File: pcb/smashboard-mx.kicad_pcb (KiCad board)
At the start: 2 copper layers, 139.1 x 76.2 mm, 87 parts, among them J1 OLED_128x32_Nice_View, SW1 SW_SPDT, SW2 SW_Push, SW3 SW_SPDT, SW4 SW_Push, U1 Nice_Nano_V2

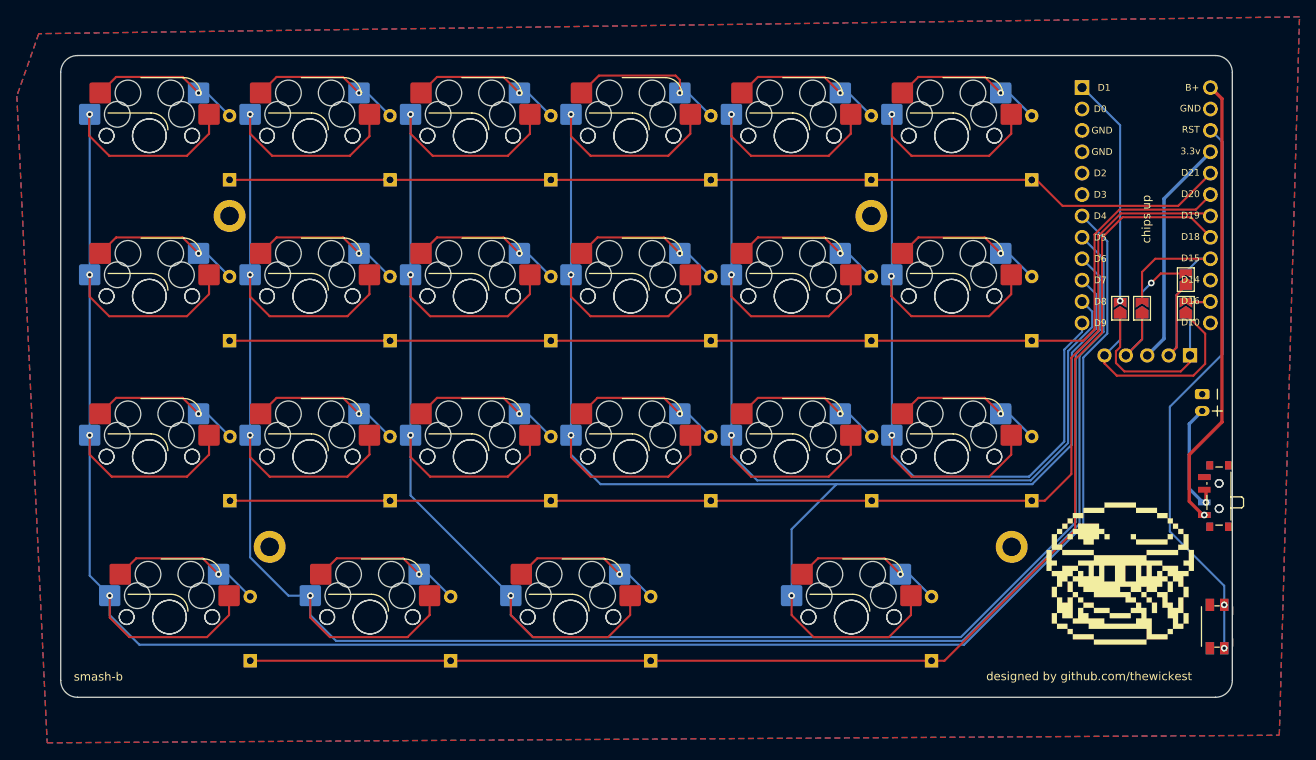
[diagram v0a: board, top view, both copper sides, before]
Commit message: Move 2u diode to the side. Interference with the stab
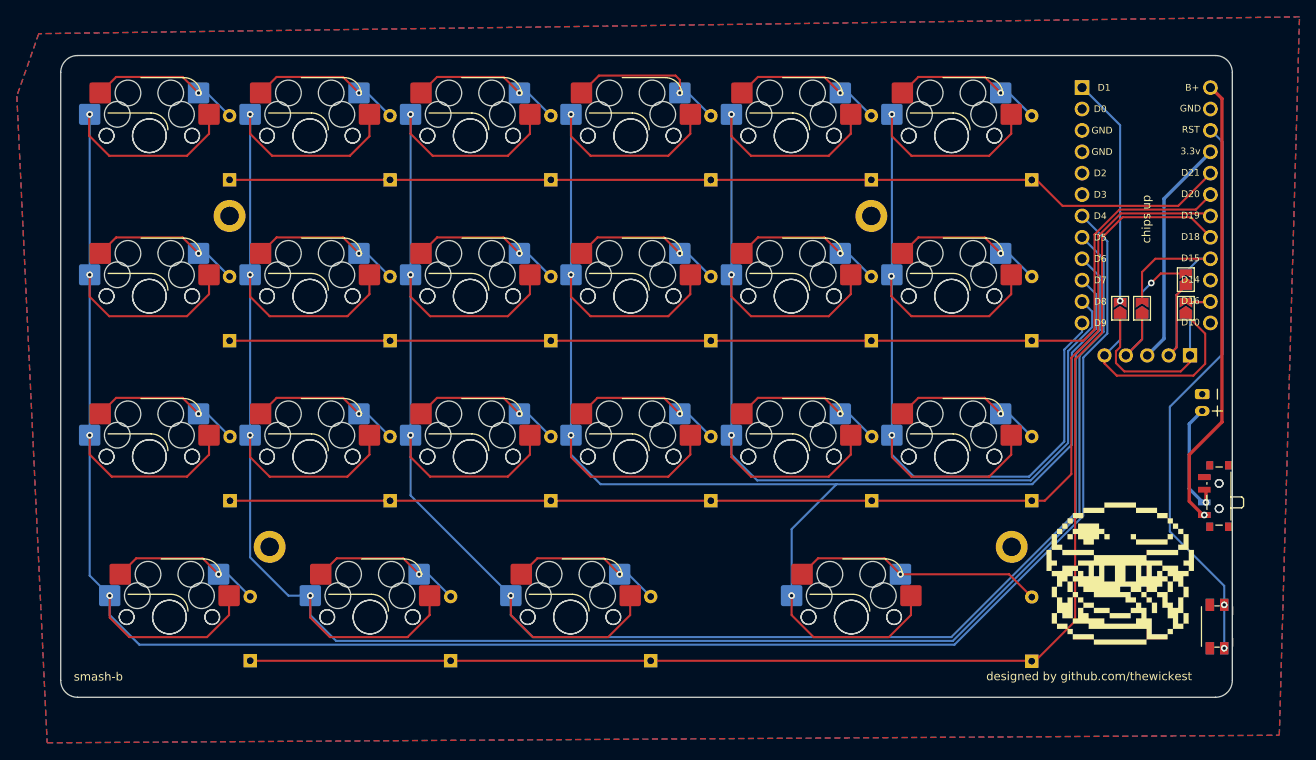
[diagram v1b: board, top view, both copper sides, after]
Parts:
- moved D22 11.9 mm to (197.0, 126.2)
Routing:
- net Net-(D22-A): track 18.0 -> 31.0 mm
- net Row4: track 155.8 -> 162.1 mm
- net Column3: track 255.7 -> 255.0 mm
- net Column2: track 283.0 -> 282.4 mm
- net Column1: track 306.7 -> 306.0 mm
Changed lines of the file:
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@@
   (setup
     (pad_to_mask_clearance 0)
-    (grid_origin 191.85875 128.1225)
+    (grid_origin 101.75875 63.24625)
     (pcbplotparams
       (layerselection 0x00010fc_ffffffff)
@@
   )
   (footprint "ScottoKeebs_Components:Diode_DO-35" (layer "B.Cu")
-    (at 185.10875 126.15625 90)
+    (at 197.00875 126.20625 90)
     (descr "Diode, DO-35_SOD27 series, Axial, Horizontal, pin pitch=7.62mm, , length*diameter=4*2mm^2, , http://www.diodes.com/_files/packages/DO-35.pdf")
     (tags "Diode DO-35_SOD27 series Axial Horizontal pin pitch 7.62mm  length 4mm diameter 2mm")
@@
   (segment (start 193.32575 96.8375) (end 194.31 96.8375) (width 0.25) (layer "B.Cu") (net 21))
   (segment (start 194.31 96.8375) (end 197.00875 99.53625) (width 0.25) (layer "B.Cu") (net 21))
-  (segment (start 202.15875 90.365292) (end 205.35875 87.165292) (width 0.25) (layer "F.Cu") (net 22))
-  (segment (start 186.645 126.15625) (end 202.15875 110.6425) (width 0.25) (layer "F.Cu") (net 22))
-  (segment (start 207.781542 73.4925) (end 215.89125 73.4925) (width 0.25) (layer "F.Cu") (net 22))
   (segment (start 205.35875 75.915292) (end 207.781542 73.4925) (width 0.25) (layer "F.Cu") (net 22))
-  (segment (start 205.35875 87.165292) (end 205.35875 75.915292) (width 0.25) (layer "F.Cu") (net 22))
-  (segment (start 217.86875 75.8825) (end 218.28125 75.8825) (width 0.25) (layer "F.Cu") (net 22))
-  (segment (start 202.15875 110.6425) (end 202.15875 90.365292) (width 0.25) (layer "F.Cu") (net 22))
+  (segment (start 104.20875 126.15625) (end 197.44875 126.15625) (width 0.25) (layer "F.Cu") (net 22))
   (segment (start 215.89125 73.4925) (end 218.28125 75.8825) (width 0.25) (layer "F.Cu") (net 22))
-  (segment (start 104.20875 126.15625) (end 185.10875 126.15625) (width 0.25) (layer "F.Cu") (net 22))
-  (segment (start 185.10875 126.15625) (end 186.645 126.15625) (width 0.25) (layer "F.Cu") (net 22))
+  (segment (start 202.15875 121.44625) (end 202.15875 90.365292) (width 0.25) (layer "F.Cu") (net 22))
+  (segment (start 202.15875 90.365292) (end 205.35875 87.165292) (width 0.25) (layer "F.Cu") (net 22))
+  (segment (start 205.35875 87.165292) (end 205.35875 75.915292) (width 0.25) (layer "F.Cu") (net 22))
+  (segment (start 207.781542 73.4925) (end 215.89125 73.4925) (width 0.25) (layer "F.Cu") (net 22))
+  (segment (start 197.44875 126.15625) (end 202.15875 121.44625) (width 0.25) (layer "F.Cu") (net 22))
+  (segment (start 218.28125 75.8825) (end 217.86875 75.8825) (width 0.25) (layer "F.Cu") (net 22))
   (segment (start 100.457 115.8875) (end 98.557 113.9875) (width 0.25) (layer "F.Cu") (net 23))
   (segment (start 90.673 113.9875) (end 88.773 115.8875) (width 0.25) (layer "F.Cu") (net 23))
@@
   (via (at 85.14875 80.3275) (size 0.8) (drill 0.4) (layers "F.Cu" "B.Cu") (net 25))
   (via (at 85.14875 99.3775) (size 0.8) (drill 0.4) (layers "F.Cu" "B.Cu") (net 25))
-  (segment (start 91.048483 124.24875) (end 188.965 124.24875) (width 0.25) (layer "B.Cu") (net 25))
-  (segment (start 203.12125 110.0925) (end 203.12125 90.145729) (width 0.25) (layer "B.Cu") (net 25))
+  (segment (start 205.9813 76.3438) (end 202.98 73.3425) (width 0.25) (layer "B.Cu") (net 25))
+  (segment (start 187.829042 124.24875) (end 203.12125 108.956542) (width 0.25) (layer "B.Cu") (net 25))
   (segment (start 85.14875 116.04625) (end 87.53 118.4275) (width 0.25) (layer "B.Cu") (net 25))
+  (segment (start 205.9813 87.285679) (end 205.9813 76.3438) (width 0.25) (layer "B.Cu") (net 25))
+  (segment (start 203.12125 108.956542) (end 203.12125 90.145729) (width 0.25) (layer "B.Cu") (net 25))
+  (segment (start 87.53 118.4275) (end 87.53 120.730267) (width 0.25) (layer "B.Cu") (net 25))
   (segment (start 87.53 120.730267) (end 91.048483 124.24875) (width 0.25) (layer "B.Cu") (net 25))
-  (segment (start 205.9813 76.3438) (end 202.98 73.3425) (width 0.25) (layer "B.Cu") (net 25))
-  (segment (start 188.965 124.24875) (end 203.12125 110.0925) (width 0.25) (layer "B.Cu") (net 25))
   (segment (start 85.14875 61.2775) (end 85.14875 116.04625) (width 0.25) (layer "B.Cu") (net 25))
   (segment (start 203.12125 90.145729) (end 205.9813 87.285679) (width 0.25) (layer "B.Cu") (net 25))
-  (segment (start 87.53 118.4275) (end 87.53 120.730267) (width 0.25) (layer "B.Cu") (net 25))
-  (segment (start 205.9813 87.285679) (end 205.9813 76.3438) (width 0.25) (layer "B.Cu") (net 25))
+  (segment (start 91.048483 124.24875) (end 187.829042 124.24875) (width 0.25) (layer "B.Cu") (net 25))
   (segment (start 115.750267 104.29875) (end 106.52125 104.29875) (width 0.25) (layer "F.Cu") (net 26))
   (segment (start 118.36875 63.87625) (end 118.36875 61.2775) (width 0.25) (layer "F.Cu") (net 26))
@@
   (via (at 111.3425 118.4275) (size 0.8) (drill 0.4) (layers "F.Cu" "B.Cu") (net 26))
   (via (at 104.19875 99.3775) (size 0.8) (drill 0.4) (layers "F.Cu" "B.Cu") (net 26))
-  (segment (start 104.19875 113.8825) (end 108.74375 118.4275) (width 0.25) (layer "B.Cu") (net 26))
-  (segment (start 202.67125 109.906104) (end 202.67125 89.959333) (width 0.25) (layer "B.Cu") (net 26))
-  (segment (start 202.67125 89.959333) (end 205.5313 87.099283) (width 0.25) (layer "B.Cu") (net 26))
   (segment (start 205.5313 78.4338) (end 202.98 75.8825) (width 0.25) (layer "B.Cu") (net 26))
-  (segment (start 188.778604 123.79875) (end 202.67125 109.906104) (width 0.25) (layer "B.Cu") (net 26))
-  (segment (start 114.410983 123.79875) (end 188.778604 123.79875) (width 0.25) (layer "B.Cu") (net 26))
+  (segment (start 104.19875 113.8825) (end 108.74375 118.4275) (width 0.25) (layer "B.Cu") (net 26))
   (segment (start 111.3425 118.4275) (end 111.3425 120.730267) (width 0.25) (layer "B.Cu") (net 26))
+  (segment (start 114.410983 123.79875) (end 187.642646 123.79875) (width 0.25) (layer "B.Cu") (net 26))
+  (segment (start 111.3425 120.730267) (end 114.410983 123.79875) (width 0.25) (layer "B.Cu") (net 26))
+  (segment (start 187.642646 123.79875) (end 202.67125 108.770146) (width 0.25) (layer "B.Cu") (net 26))
+  (segment (start 202.67125 89.959333) (end 205.5313 87.099283) (width 0.25) (layer "B.Cu") (net 26))
   (segment (start 104.19875 61.2775) (end 104.19875 113.8825) (width 0.25) (layer "B.Cu") (net 26))
   (segment (start 108.74375 118.4275) (end 111.3425 118.4275) (width 0.25) (layer "B.Cu") (net 26))
-  (segment (start 111.3425 120.730267) (end 114.410983 123.79875) (width 0.25) (layer "B.Cu") (net 26))
+  (segment (start 202.67125 108.770146) (end 202.67125 89.959333) (width 0.25) (layer "B.Cu") (net 26))
   (segment (start 205.5313 87.099283) (end 205.5313 78.4338) (width 0.25) (layer "B.Cu") (net 26))
   (segment (start 146.706517 123.34875) (end 137.773483 123.34875) (width 0.25) (layer "F.Cu") (net 27))
@@
   (via (at 135.155 118.4275) (size 0.8) (drill 0.4) (layers "F.Cu" "B.Cu") (net 27))
   (via (at 123.24875 80.3275) (size 0.8) (drill 0.4) (layers "F.Cu" "B.Cu") (net 27))
+  (segment (start 135.155 120.730267) (end 137.773483 123.34875) (width 0.25) (layer "B.Cu") (net 27))
+  (segment (start 202.22125 89.772937) (end 205.0813 86.912887) (width 0.25) (layer "B.Cu") (net 27))
   (segment (start 123.24875 61.2775) (end 123.24875 106.52125) (width 0.25) (layer "B.Cu") (net 27))
+  (segment (start 202.22125 108.58375) (end 202.22125 89.772937) (width 0.25) (layer "B.Cu") (net 27))
   (segment (start 205.0813 80.5238) (end 202.98 78.4225) (width 0.25) (layer "B.Cu") (net 27))
-  (segment (start 188.592208 123.34875) (end 202.22125 109.719708) (width 0.25) (layer "B.Cu") (net 27))
-  (segment (start 135.155 118.4275) (end 135.155 120.730267) (width 0.25) (layer "B.Cu") (net 27))
-  (segment (start 202.22125 89.772937) (end 205.0813 86.912887) (width 0.25) (layer "B.Cu") (net 27))
-  (segment (start 137.773483 123.34875) (end 188.592208 123.34875) (width 0.25) (layer "B.Cu") (net 27))
-  (segment (start 205.0813 86.912887) (end 205.0813 80.5238) (width 0.25) (layer "B.Cu") (net 27))
   (segment (start 123.24875 106.52125) (end 135.155 118.4275) (width 0.25) (layer "B.Cu") (net 27))
-  (segment (start 202.22125 109.719708) (end 202.22125 89.772937) (width 0.25) (layer "B.Cu") (net 27))
-  (segment (start 135.155 120.730267) (end 137.773483 123.34875) (width 0.25) (layer "B.Cu") (net 27))
+  (segment (start 187.45625 123.34875) (end 202.22125 108.58375) (width 0.25) (layer "B.Cu") (net 27))
+  (segment (start 137.773483 123.34875) (end 187.45625 123.34875) (width 0.25) (layer "B.Cu") (net 27))
+  (segment (start 205.0813 86.912887) (end 205.0813 80.5238) (width 0.25) (layer "B.Cu") (net 27))
+  (segment (start 135.155 118.4275) (end 135.155 120.730267) (width 0.25) (layer "B.Cu") (net 27))
   (segment (start 156.46875 82.630267) (end 153.850267 85.24875) (width 0.25) (layer "F.Cu") (net 28))
   (segment (start 142.29875 101.97625) (end 142.29875 99.3775) (width 0.25) (layer "F.Cu") (net 28))
@@
   (segment (start 149.11625 115.8875) (end 151.765 118.53625) (width 0.25) (layer "B.Cu") (net 36))
   (segment (start 148.082 115.8875) (end 149.11625 115.8875) (width 0.25) (layer "B.Cu") (net 36))
+  (segment (start 181.4195 115.8875) (end 194.31 115.8875) (width 0.25) (layer "F.Cu") (net 37))
+  (segment (start 194.31 115.8875) (end 197.00875 118.58625) (width 0.25) (layer "F.Cu") (net 37))
   (segment (start 181.4195 115.8875) (end 179.5195 113.9875) (width 0.25) (layer "F.Cu") (net 37))
   (segment (start 171.6355 113.9875) (end 169.7355 115.8875) (width 0.25) (layer "F.Cu") (net 37))
   (segment (start 179.5195 113.9875) (end 171.6355 113.9875) (width 0.25) (layer "F.Cu") (net 37))
   (via (at 181.4195 115.8875) (size 0.8) (drill 0.4) (layers "F.Cu" "B.Cu") (net 37))
-  (segment (start 182.46 115.8875) (end 185.10875 118.53625) (width 0.25) (layer "B.Cu") (net 37))
   (segment (start 181.4195 115.8875) (end 182.46 115.8875) (width 0.25) (layer "B.Cu") (net 37))
   (segment (start 207.5 83.575) (end 207.5 83.425) (width 0.25) (layer "F.Cu") (net 38))
